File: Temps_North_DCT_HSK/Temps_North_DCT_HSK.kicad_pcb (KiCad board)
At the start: 2 copper layers, 53.3 x 57.1 mm, 6 parts, among them J1 North_Temps_1, J2 North_Temps_2, J3 Internal_Temps_DCT_HSK_Box_1, J4 Internal_Temps_DCT_HSK_Box_2

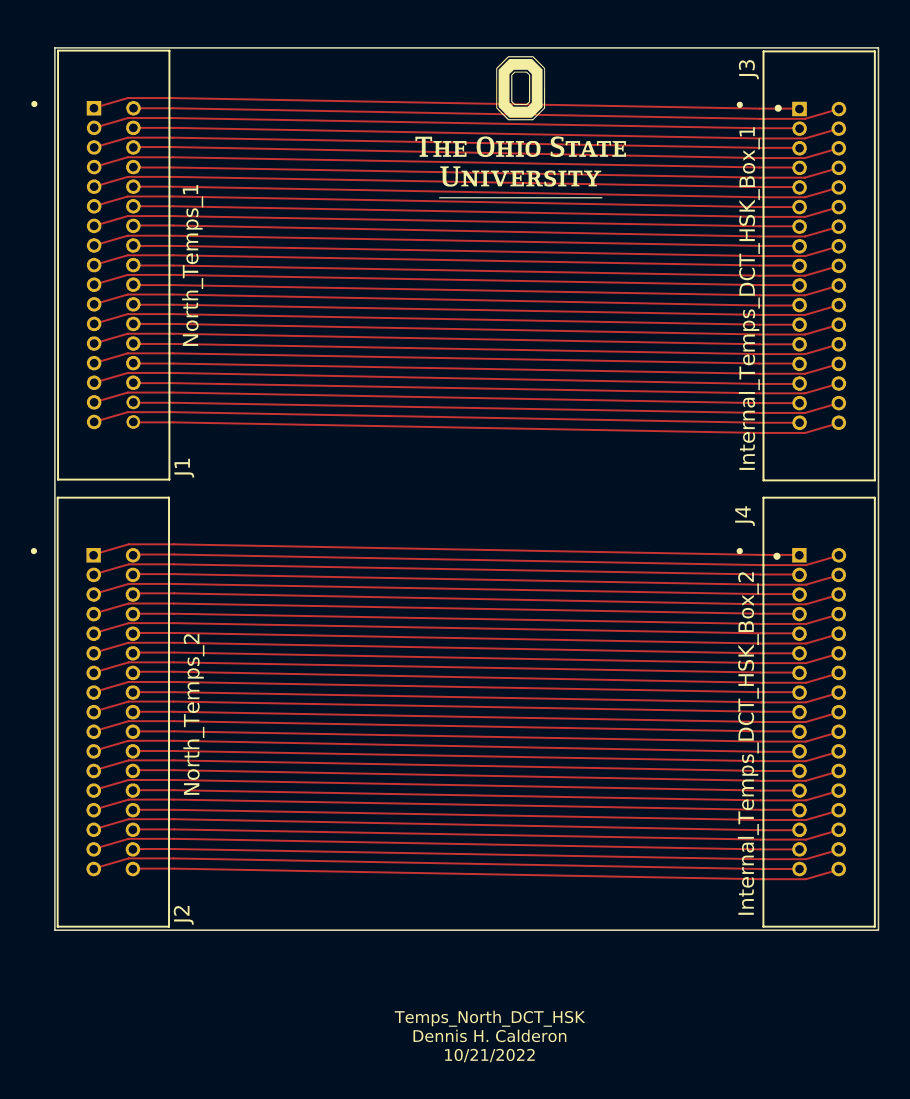
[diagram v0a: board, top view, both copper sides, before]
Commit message: Corrected pinout for from NTB2 to DCT HSK
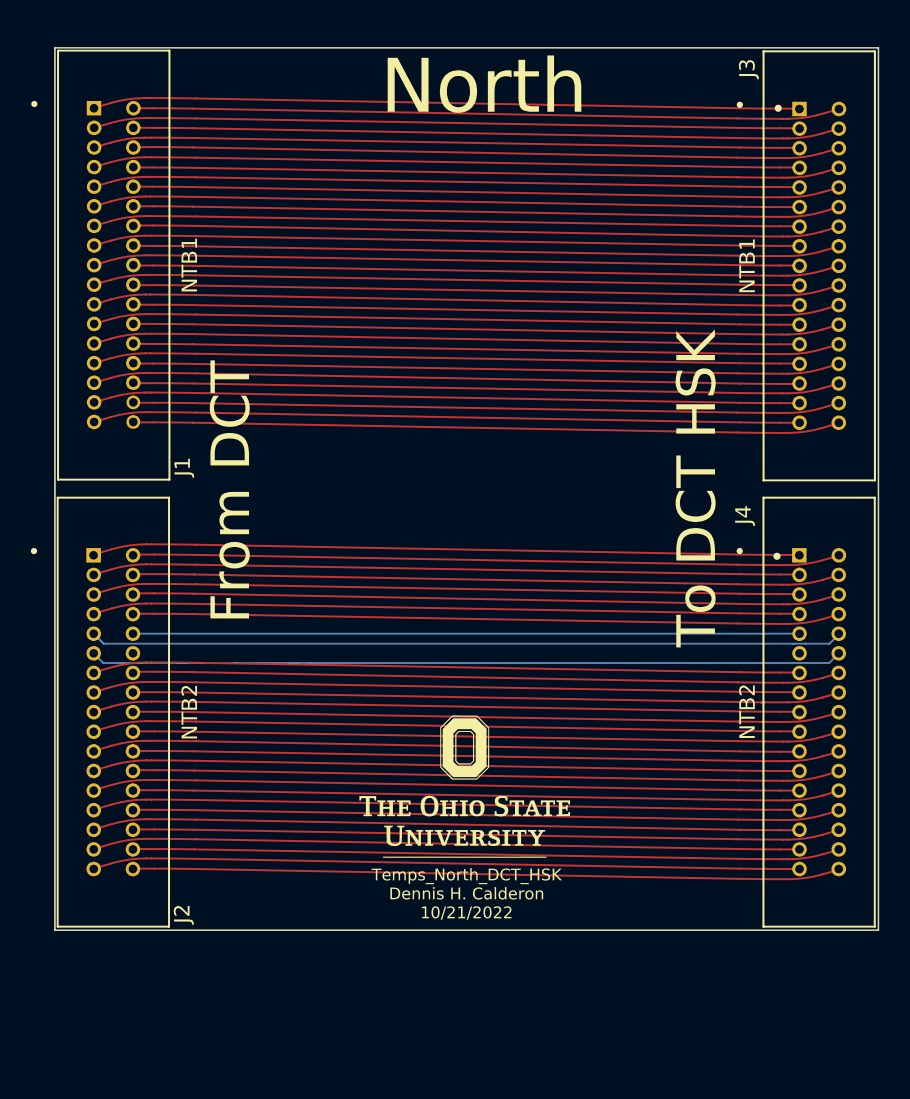
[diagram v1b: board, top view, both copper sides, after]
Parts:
- moved G*** 42.9 mm to (118.0, 94.8)
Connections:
- J2 pad 10: (no net) -> /TD2_10
- J2 pad 11: (no net) -> /TD2_11
- J2 pad 12: (no net) -> unconnected-(J2-Pad12)
- J2 pad 13: (no net) -> /TD2_13
- J2 pad 14: (no net) -> /TD2_14
- J2 pad 15: (no net) -> /TD2_15
- J2 pad 16: (no net) -> /TD2_16
- J2 pad 17: (no net) -> /TD2_17
- J2 pad 18: (no net) -> /TD2_18
- J2 pad 19: (no net) -> /TD2_19
- J2 pad 20: (no net) -> /TD2_20
- J2 pad 21: (no net) -> /TD2_21
- J2 pad 22: (no net) -> /TD2_22
- J2 pad 23: (no net) -> /TD2_23
- J2 pad 24: (no net) -> /TD2_24
- J2 pad 25: (no net) -> /TD2_25
- J2 pad 26: (no net) -> /TD2_26
- J2 pad 27: (no net) -> /TD2_27
- J2 pad 28: (no net) -> /TD2_28
- J2 pad 29: (no net) -> /TD2_29
- J2 pad 3: (no net) -> /TD2_3
- J2 pad 30: (no net) -> /TD2_30
- J2 pad 31: (no net) -> /TD2_31
- J2 pad 32: (no net) -> /TD2_32
- J2 pad 33: (no net) -> /TD2_33
- J2 pad 34: (no net) -> /TD2_34
- J2 pad 4: (no net) -> /TD2_4
- J2 pad 5: (no net) -> /TD2_5
- J2 pad 6: (no net) -> /TD2_6
- J2 pad 7: (no net) -> /TD2_7
- J2 pad 8: (no net) -> /TD2_8
- J2 pad 9: (no net) -> /TD2_9
- J4 pad 1: (no net) -> /TD2_1
- J4 pad 10: (no net) -> /TD2_9
- J4 pad 11: (no net) -> unconnected-(J4-Pad11)
- J4 pad 12: (no net) -> /TD2_11
- J4 pad 13: (no net) -> /TD2_13
- J4 pad 14: (no net) -> /TD2_14
- J4 pad 15: (no net) -> /TD2_15
- J4 pad 16: (no net) -> /TD2_16
- J4 pad 17: (no net) -> /TD2_17
- J4 pad 18: (no net) -> /TD2_18
- J4 pad 19: (no net) -> /TD2_19
- J4 pad 2: (no net) -> /TD2_2
- J4 pad 20: (no net) -> /TD2_20
- J4 pad 21: (no net) -> /TD2_21
- J4 pad 22: (no net) -> /TD2_22
- J4 pad 23: (no net) -> /TD2_23
- J4 pad 24: (no net) -> /TD2_24
- J4 pad 25: (no net) -> /TD2_25
- J4 pad 26: (no net) -> /TD2_26
- J4 pad 27: (no net) -> /TD2_27
- J4 pad 28: (no net) -> /TD2_28
- J4 pad 29: (no net) -> /TD2_29
- J4 pad 3: (no net) -> /TD2_3
- J4 pad 30: (no net) -> /TD2_30
- J4 pad 31: (no net) -> /TD2_31
- J4 pad 32: (no net) -> /TD2_32
- J4 pad 33: (no net) -> /TD2_33
- J4 pad 34: (no net) -> /TD2_34
- J4 pad 4: (no net) -> /TD2_4
- J4 pad 5: (no net) -> /TD2_5
- J4 pad 6: (no net) -> /TD2_6
- J4 pad 7: (no net) -> /TD2_7
- J4 pad 8: (no net) -> /TD2_8
- J4 pad 9: (no net) -> /TD2_10
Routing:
- net (no net): track 1465.1 -> 0.00 mm
- net /TD2_11: track 0.00 -> 48.8 mm
- net /TD2_9: track 0.00 -> 48.8 mm
- net /TD2_16: track 0.00 -> 45.8 mm
- net /TD2_21: track 0.00 -> 45.8 mm
- net /TD2_14: track 0.00 -> 45.8 mm
- net /TD2_25: track 0.00 -> 45.8 mm
- net /TD2_23: track 0.00 -> 45.8 mm
- net /TD2_17: track 0.00 -> 45.8 mm
- net /TD2_15: track 0.00 -> 45.8 mm
- net /TD2_20: track 0.00 -> 45.8 mm
- net /TD2_18: track 0.00 -> 45.8 mm
- net /TD2_7: track 0.00 -> 45.8 mm
- net /TD2_28: track 0.00 -> 45.8 mm
- net /TD2_31: track 0.00 -> 45.8 mm
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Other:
- board text added: "From DCT"
- board text added: "NTB1"
- board text added: "NTB2"
- board text added: "North"
- board text added: "To DCT HSK"

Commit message: updated Temp boards
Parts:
- removed the G*** at (118.0, 94.8)
- removed the G*** at (125.2, 76.1)
- added G***: LOGO, LOGO, F.Cu at (127.3, 93.7)
- added G***: LOGO, LOGO, F.Cu at (127.3, 54.3)
- added G***: LOGO, LOGO, B.Cu at (129.1, 75.5)
